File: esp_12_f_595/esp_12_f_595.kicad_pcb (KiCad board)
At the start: 2 copper layers, 85.7 x 29.2 mm, 26 parts, among them P0 RGB_OUT, P1 RGB_OUT, P2 RGB_OUT, P3 CONN_01X04, P4 MicroB, P5 CONN_01X04, SW1 TACTILE, U1 74HC595, U2 74HC595, U3 AP1117v3.3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

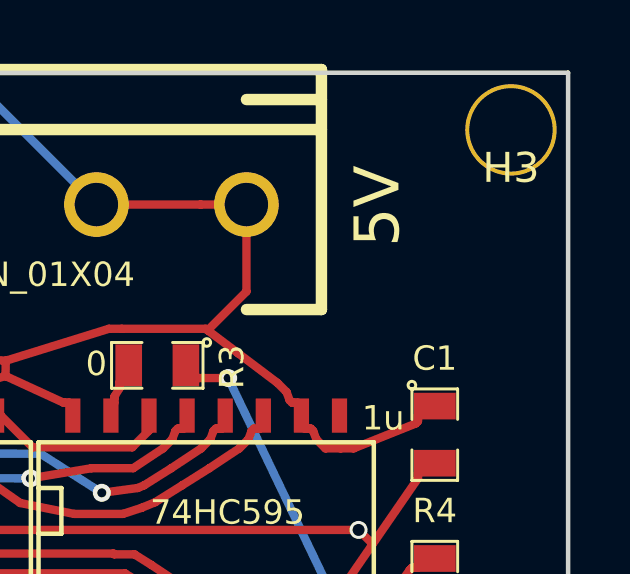
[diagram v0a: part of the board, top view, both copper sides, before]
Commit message: update with new build materials
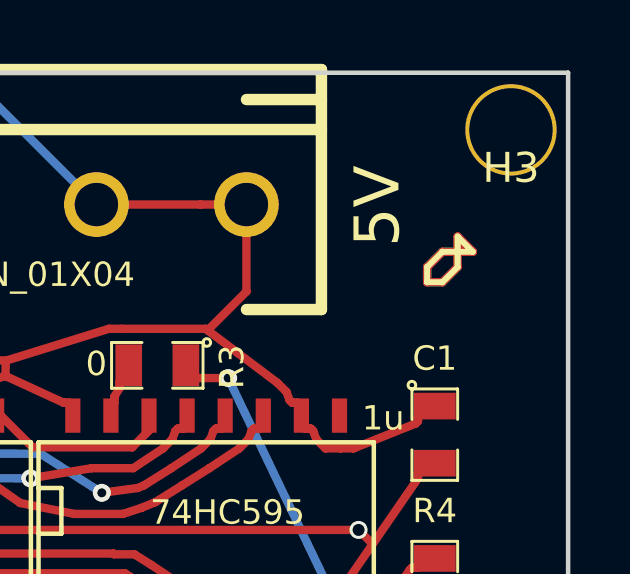
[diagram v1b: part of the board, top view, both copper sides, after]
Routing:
- net (no net): track 1.27 -> 11.7 mm
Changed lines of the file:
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@@
     (links 121)
     (no_connects 0)
-    (area 69.774999 76.759999 155.650001 106.120001)
+    (area 69.774999 68.950999 155.650001 106.539)
     (thickness 1.6)
-    (drawings 8)
-    (tracks 1148)
+    (drawings 22)
+    (tracks 1166)
     (zones 0)
     (modules 26)
@@
     (visible_elements FFFFFF7F)
     (pcbplotparams
-      (layerselection 0x00030_80000001)
-      (usegerberextensions false)
-      (excludeedgelayer true)
+      (layerselection 0x010f0_80000001)
+      (usegerberextensions true)
+      (excludeedgelayer false)
       (linewidth 0.100000)
       (plotframeref false)
@@
       (outputformat 1)
       (mirror false)
-      (drillshape 1)
+      (drillshape 0)
       (scaleselection 1)
-      (outputdirectory ""))
+      (outputdirectory esp_12_f_595))
   )
   (net 0 "")
@@
       (net 2 GND))
   )
+  (gr_line (start 151.384 82.804) (end 152.4 82.804) (angle 90) (layer F.SilkS) (width 0.2))
+  (gr_line (start 150.876 83.312) (end 151.384 82.804) (angle 90) (layer F.SilkS) (width 0.2))
+  (gr_line (start 150.876 83.82) (end 150.876 83.312) (angle 90) (layer F.SilkS) (width 0.2))
+  (gr_line (start 151.384 83.82) (end 150.876 83.82) (angle 90) (layer F.SilkS) (width 0.2))
+  (gr_line (start 151.892 83.312) (end 151.384 83.82) (angle 90) (layer F.SilkS) (width 0.2))
+  (gr_line (start 151.892 82.296) (end 151.892 83.312) (angle 90) (layer F.SilkS) (width 0.2))
+  (gr_line (start 152.4 82.804) (end 151.892 82.296) (angle 90) (layer F.SilkS) (width 0.2))
+  (gr_line (start 151.384 82.804) (end 152.4 82.804) (angle 90) (layer B.SilkS) (width 0.2))
+  (gr_line (start 150.876 83.312) (end 151.384 82.804) (angle 90) (layer B.SilkS) (width 0.2))
+  (gr_line (start 150.876 83.82) (end 150.876 83.312) (angle 90) (layer B.SilkS) (width 0.2))
+  (gr_line (start 151.384 83.82) (end 150.876 83.82) (angle 90) (layer B.SilkS) (width 0.2))
+  (gr_line (start 151.892 83.312) (end 151.384 83.82) (angle 90) (layer B.SilkS) (width 0.2))
+  (gr_line (start 151.892 82.296) (end 151.892 83.312) (angle 90) (layer B.SilkS) (width 0.2))
+  (gr_line (start 152.4 82.804) (end 151.892 82.296) (angle 90) (layer B.SilkS) (width 0.2))
   (gr_text 5V (at 149.225 81.28 90) (layer F.SilkS)
     (effects (font (size 1.5 1.5) (thickness 0.3)))
@@
   (gr_line (start 113.665 76.835) (end 155.575 76.835) (layer Edge.Cuts) (width 0.15))
   (gr_line (start 69.85 76.835) (end 113.665 76.835) (layer Edge.Cuts) (width 0.15))
+  (segment (start 150.876 83.82) (end 150.876 83.312) (width 0.2794) (layer B.Cu) (net 0))
+  (segment (start 151.384 83.82) (end 150.876 83.82) (width 0.2794) (layer B.Cu) (net 0))
+  (segment (start 151.892 83.312) (end 151.384 83.82) (width 0.2794) (layer B.Cu) (net 0))
+  (segment (start 151.892 82.804) (end 151.892 83.312) (width 0.2794) (layer B.Cu) (net 0))
+  (segment (start 151.384 82.804) (end 151.892 82.804) (width 0.2794) (layer B.Cu) (net 0))
+  (segment (start 150.876 83.312) (end 151.384 82.804) (width 0.2794) (layer B.Cu) (net 0))
+  (segment (start 151.892 82.804) (end 151.892 82.296) (width 0.2794) (layer B.Cu) (net 0))
+  (segment (start 151.892 82.296) (end 152.4 82.804) (width 0.2794) (layer B.Cu) (net 0))
+  (segment (start 152.4 82.804) (end 151.892 82.804) (width 0.2794) (layer B.Cu) (net 0))
   (via (at 109.855 93.345) (size 0.6) (drill 0.4) (layers F.Cu B.Cu) (net 0))
   (segment (start 90.17 93.98) (end 91.44 93.98) (width 0.2794) (layer B.Cu) (net 0))
   (via (at 91.44 93.98) (size 0.6) (drill 0.4) (layers F.Cu B.Cu) (net 0))
+  (segment (start 150.876 83.82) (end 150.876 83.312) (width 0.2794) (layer F.Cu) (net 0))
+  (segment (start 151.384 83.82) (end 150.876 83.82) (width 0.2794) (layer F.Cu) (net 0))
+  (segment (start 151.892 83.312) (end 151.384 83.82) (width 0.2794) (layer F.Cu) (net 0))
+  (segment (start 151.892 82.804) (end 151.892 83.312) (width 0.2794) (layer F.Cu) (net 0))
+  (segment (start 151.384 82.804) (end 151.892 82.804) (width 0.2794) (layer F.Cu) (net 0))
+  (segment (start 150.876 83.312) (end 151.384 82.804) (width 0.2794) (layer F.Cu) (net 0))
+  (segment (start 151.892 82.804) (end 151.892 82.296) (width 0.2794) (layer F.Cu) (net 0))
+  (segment (start 151.892 82.296) (end 152.4 82.804) (width 0.2794) (layer F.Cu) (net 0))
+  (segment (start 152.4 82.804) (end 151.892 82.804) (width 0.2794) (layer F.Cu) (net 0))
   (segment (start 139.8524 81.2292) (end 136.168478 77.545278) (width 0.2794) (layer B.Cu) (net 1))
   (segment (start 136.168478 77.545278) (end 118.382464 77.545278) (width 0.2794) (layer B.Cu) (net 1))
